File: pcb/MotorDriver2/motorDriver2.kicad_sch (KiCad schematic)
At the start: 2 parts

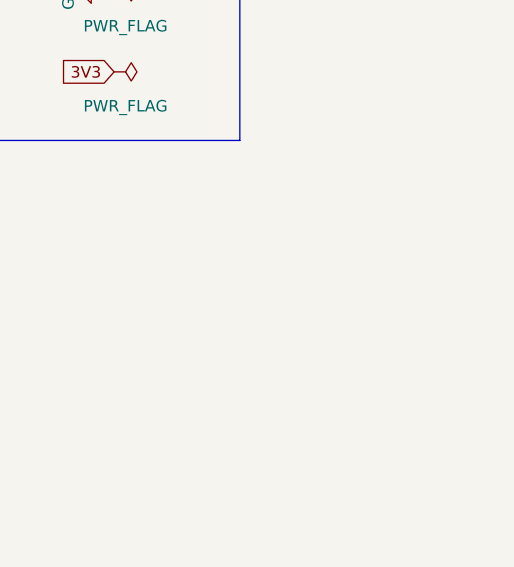
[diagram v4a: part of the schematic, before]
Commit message: Removed can transceivers, replaced with spi
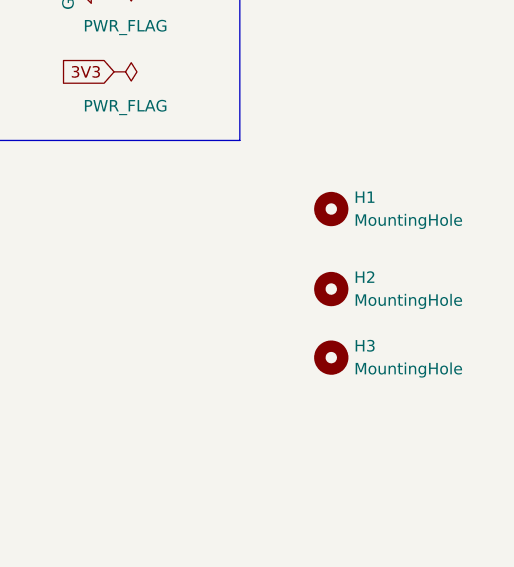
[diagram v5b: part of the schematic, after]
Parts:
- added H1, H2, H3: MountingHole, MountingHole:ToolingHole_1.152mm, symbol Mechanical:MountingHole
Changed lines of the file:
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@@
+	)
+	(symbol
+		(lib_id "Mechanical:MountingHole")
+		(at 199.39 154.94 0)
+		(unit 1)
+		(exclude_from_sim no)
+		(in_bom no)
+		(on_board yes)
+		(dnp no)
+		(fields_autoplaced yes)
+		(property "Reference" "H3"
+			(at 201.93 153.6699 0)
+			(effects
+				(font
+					(size 1.27 1.27)
+				)
+				(justify left)
+			)
+		)
+		(property "Value" "MountingHole"
+			(at 201.93 156.2099 0)
+			(effects
+				(font
+					(size 1.27 1.27)
+				)
+				(justify left)
+			)
+		)
+		(property "Footprint" "MountingHole:ToolingHole_1.152mm"
+			(at 199.39 154.94 0)
+			(effects
+				(font
+					(size 1.27 1.27)
+				)
+				(hide yes)
+			)
+		)
+		(property "Datasheet" "~"
+			(at 199.39 154.94 0)
+			(effects
+				(font
+					(size 1.27 1.27)
+				)
+				(hide yes)
+			)
+		)
+		(property "Description" "Mounting Hole without connection"
+			(at 199.39 154.94 0)
+			(effects
+				(font
+					(size 1.27 1.27)
+				)
+				(hide yes)
+			)
+		)
+		(instances
+			(project "MotorDriver2"
+				(path "/6e0510ec-6dbc-4bc1-a315-3680b1127a92"
+					(reference "H3")
+					(unit 1)
+				)
+			)
+		)
+	)
+	(symbol
+		(lib_id "Mechanical:MountingHole")
+		(at 199.39 138.43 0)
+		(unit 1)
+		(exclude_from_sim no)
+		(in_bom no)
+		(on_board yes)
+		(dnp no)
+		(fields_autoplaced yes)
+		(property "Reference" "H1"
+			(at 201.93 137.1599 0)
+			(effects
+				(font
+					(size 1.27 1.27)
+				)
+				(justify left)
+			)
+		)
+		(property "Value" "MountingHole"
+			(at 201.93 139.6999 0)
+			(effects
+				(font
+					(size 1.27 1.27)
+				)
+				(justify left)
+			)
+		)
+		(property "Footprint" "MountingHole:ToolingHole_1.152mm"
+			(at 199.39 138.43 0)
+			(effects
+				(font
+					(size 1.27 1.27)
+				)
+				(hide yes)
+			)
+		)
+		(property "Datasheet" "~"
+			(at 199.39 138.43 0)
+			(effects
+				(font
+					(size 1.27 1.27)
+				)
+				(hide yes)
+			)
+		)
+		(property "Description" "Mounting Hole without connection"
+			(at 199.39 138.43 0)
+			(effects
+				(font
+					(size 1.27 1.27)
+				)
+				(hide yes)
+			)
+		)
+		(instances
+			(project ""
+				(path "/6e0510ec-6dbc-4bc1-a315-3680b1127a92"
+					(reference "H1")
+					(unit 1)
+				)
+			)
+		)
 	)
 	(symbol
@@
 	)
 	(symbol
+		(lib_id "Mechanical:MountingHole")
+		(at 199.39 147.32 0)
+		(unit 1)
+		(exclude_from_sim no)
+		(in_bom no)
+		(on_board yes)
+		(dnp no)
+		(fields_autoplaced yes)
+		(property "Reference" "H2"
+			(at 201.93 146.0499 0)
+			(effects
+				(font
+					(size 1.27 1.27)
+				)
+				(justify left)
+			)
+		)
+		(property "Value" "MountingHole"
+			(at 201.93 148.5899 0)
+			(effects
+				(font
+					(size 1.27 1.27)
+				)
+				(justify left)
+			)
+		)
+		(property "Footprint" "MountingHole:ToolingHole_1.152mm"
+			(at 199.39 147.32 0)
+			(effects
+				(font
+					(size 1.27 1.27)
+				)
+				(hide yes)
+			)
+		)
+		(property "Datasheet" "~"
+			(at 199.39 147.32 0)
+			(effects
+				(font
+					(size 1.27 1.27)
+				)
+				(hide yes)
+			)
+		)
+		(property "Description" "Mounting Hole without connection"
+			(at 199.39 147.32 0)
+			(effects
+				(font
+					(size 1.27 1.27)
+				)
+				(hide yes)
+			)
+		)
+		(instances
+			(project "MotorDriver2"
+				(path "/6e0510ec-6dbc-4bc1-a315-3680b1127a92"
+					(reference "H2")
+					(unit 1)
+				)
+			)
+		)
+	)
+	(symbol
 		(lib_id "power:PWR_FLAG")
 		(at 175.26 123.19 270)
@@
 		)
 		(instances
-			(project "motorDriver2"
+			(project "MotorDriver2"
 				(path "/6e0510ec-6dbc-4bc1-a315-3680b1127a92"
 					(page "6")
@@
 		)
 		(instances
-			(project "motorDriver2"
+			(project "MotorDriver2"
 				(path "/6e0510ec-6dbc-4bc1-a315-3680b1127a92"
 					(page "7")
@@
 		)
 		(instances
-			(project "motorDriver2"
+			(project "MotorDriver2"
 				(path "/6e0510ec-6dbc-4bc1-a315-3680b1127a92"
 					(page "8")
@@
 		)
 		(instances
-			(project "motorDriver2"
+			(project "MotorDriver2"
 				(path "/6e0510ec-6dbc-4bc1-a315-3680b1127a92"
 					(page "4")
@@
 		)
 		(instances
-			(project "motorDriver2"
+			(project "MotorDriver2"
 				(path "/6e0510ec-6dbc-4bc1-a315-3680b1127a92"
 					(page "5")
@@
 		)
 		(instances
-			(project "motorDriver2"
+			(project "MotorDriver2"
 				(path "/6e0510ec-6dbc-4bc1-a315-3680b1127a92"
 					(page "3")
@@
 		)
 		(instances
-			(project "motorDriver2"
+			(project "MotorDriver2"
 				(path "/6e0510ec-6dbc-4bc1-a315-3680b1127a92"
 					(page "2")
